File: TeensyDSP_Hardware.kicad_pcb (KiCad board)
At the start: 2 copper layers, 100 x 50 mm, 57 parts, among them J1 AudioJack2, J2 AudioJack2, J3 Conn_01x04_Pin, SW2 SW_DPDT_x2, SW3 SW_SPDT, U1 TL071, U2 LTC1044, U3 TL071, U4 TL071, U5 TL071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

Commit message: final commit before change to single ended
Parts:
- removed C10, C11, C12, C13, C14, C7, C8, C9: C, Capacitor_THT:C_Disc_D4.3mm_W1.9mm_P5.00mm
- removed J2: AudioJack2, Connector_Audio:Jack_3.5mm_Ledino_KB3SPRS_Horizontal
- removed R13, R14, R15, R16, R17, R18, R19: R, Resistor_THT:R_Axial_DIN0207_L6.3mm_D2.5mm_P7.62mm_Horizontal
- removed U4, U5: TL071, Package_DIP:DIP-8_W7.62mm
- removed UI_Switch_B1: SW_SPDT, Button_Switch_THT:SW_Slide-03_Wuerth-WS-SLTV_10x2.5x6.4_P2.54mm
- added R6: R, Resistor_THT:R_Axial_DIN0207_L6.3mm_D2.5mm_P7.62mm_Horizontal, F.Cu at (72.4, 101.5)
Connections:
- U6 pad 36: unconnected-(U6-14_A0_TX3_SPDIF_OUT-Pad36) -> /AD0
- U6 pad 37: unconnected-(U6-15_A1_RX3_SPDIF_IN-Pad37) -> /AD1
- U6 pad 42: unconnected-(U6-20_A6_TX5_LRCLK1-Pad42) -> /AD6
- U6 pad 43: unconnected-(U6-21_A7_RX5_BCLK1-Pad43) -> /AD7
- U6 pad 44: unconnected-(U6-22_A8_CTX1-Pad44) -> /AD8
- U6 pad 51: unconnected-(U6-3V3-Pad51) -> +3V3
- U6 pad 52: unconnected-(U6-GND-Pad52) -> GND

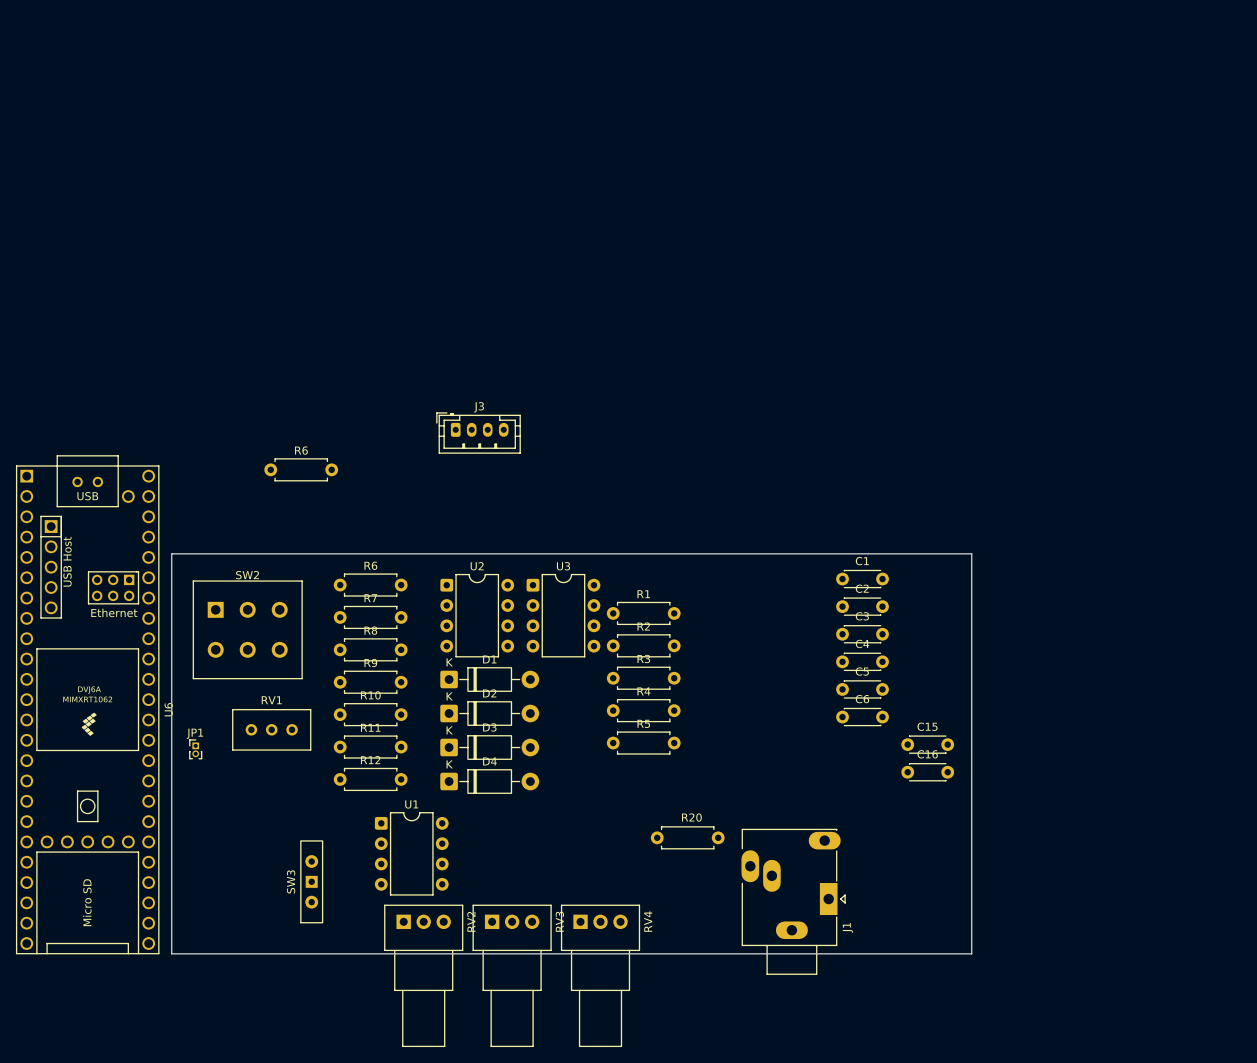
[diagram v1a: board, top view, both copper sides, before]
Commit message: First layout attempt - large footprint
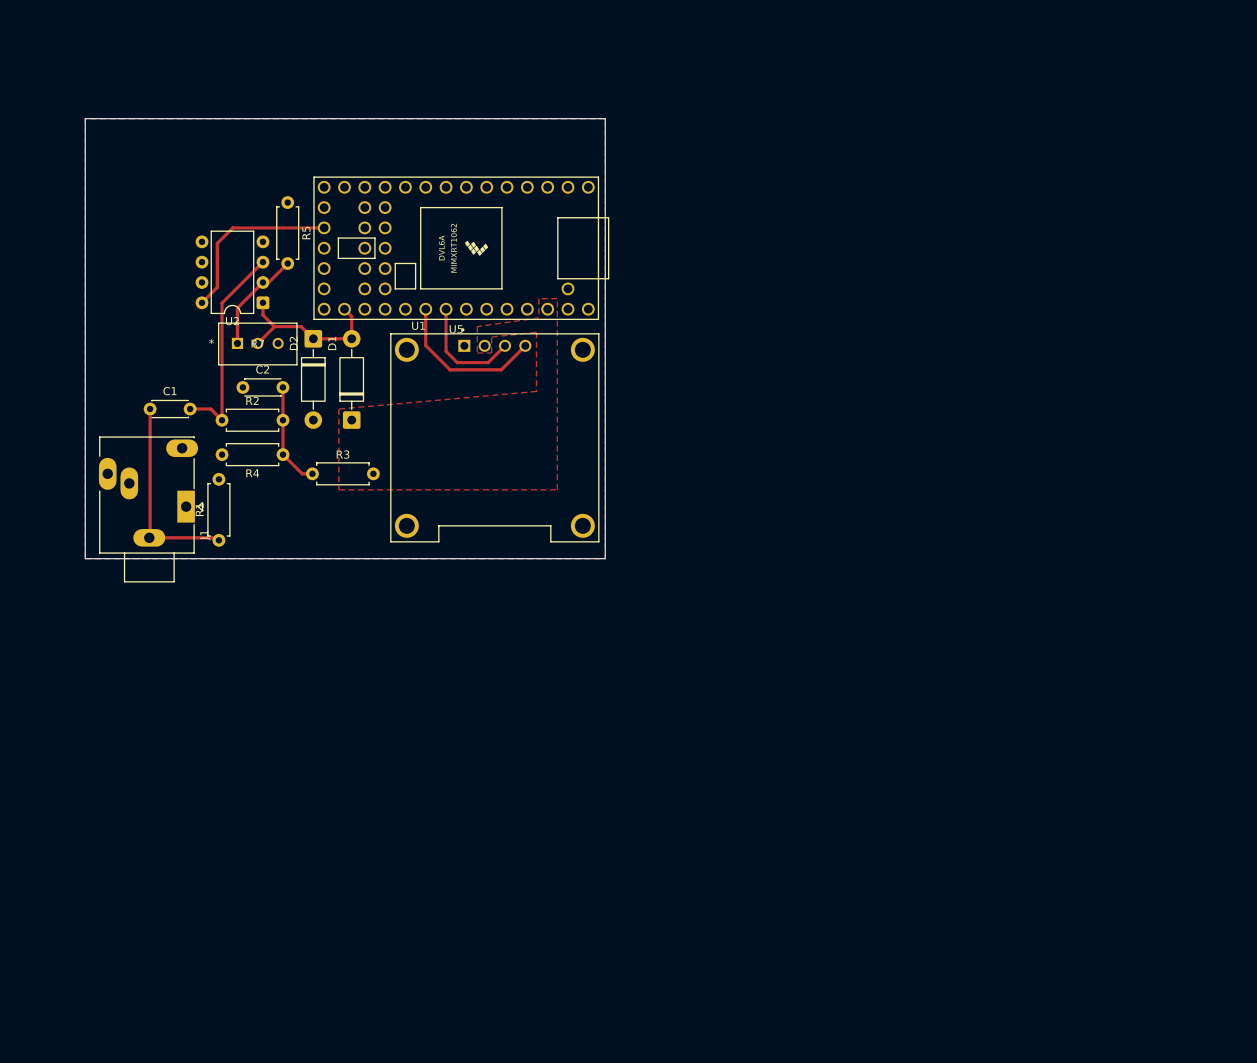
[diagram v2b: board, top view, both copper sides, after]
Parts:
- removed C15, C16, C3, C4, C5, C6: C, Capacitor_THT:C_Disc_D4.3mm_W1.9mm_P5.00mm
- removed D3, D4: 1N5817, Diode_THT:D_DO-41_SOD81_P10.16mm_Horizontal
- removed J3: Conn_01x04_Pin, Connector_JST:JST_PH_B4B-PH-K_1x04_P2.00mm_Vertical
- removed JP1: Jumper_2_Open, Connector_PinHeader_1.00mm:PinHeader_1x02_P1.00mm_Vertical
- removed R10, R11, R12, R20, R6 (x2), R8, R9: R, Resistor_THT:R_Axial_DIN0207_L6.3mm_D2.5mm_P7.62mm_Horizontal
- removed RV1: 500k, Potentiometer_THT:Potentiometer_Bourns_3296W_Vertical
- removed RV2, RV3, RV4: 500k, Potentiometer_THT:Potentiometer_Alps_RK09Y11_Single_Horizontal
- removed SW2: SW_DPDT_x2, Button_Switch_THT:SW_PUSH_E-Switch_FS5700DP_DPDT
- removed SW3: SW_SPDT, Button_Switch_THT:SW_Slide-03_Wuerth-WS-SLTV_10x2.5x6.4_P2.54mm
- removed U3: TL071, Package_DIP:DIP-8_W7.62mm
- removed U6: Teensy4.1, Teensy:Teensy41
- added U5: Teensy4.0, Teensy:Teensy40, F.Cu at (95.6, 73.8)
- C1, C2: value C -> 10u
- R1, R2: value R -> 47k
- R3: value R -> 10k
- R4: value R -> 2.2k
- R5: value R -> 1k
- R7: value R -> PV36W502C01B00; footprint Resistor_THT:R_Axial_DIN0207_L6.3mm_D2.5mm_P7.62mm_Horizontal -> MyComponents:POT_PV36W_BRN
- U1: value TL071 -> DM-OLED096-636; footprint Package_DIP:DIP-8_W7.62mm -> MyComponents:LED_SCREEN096
- U2: value LTC1044 -> TL072
- moved J1 94.1 mm to (61.8, 106.1)
- moved C1 89.1 mm to (57.3, 93.9)
- moved C2 79.8 mm to (68.9, 91.2)
- moved R5 78.9 mm to (74.5, 68.1), turned to -90 degrees
- moved R2 56.4 mm to (66.3, 95.3)
- moved R4 52.2 mm to (73.9, 99.6), turned to 180 degrees
- moved U1 50.2 mm to (100.4, 97.5)
- moved R1 50.1 mm to (65.9, 110.3), turned to 90 degrees
- moved D2 49.8 mm to (77.7, 85.1), turned to -90 degrees
- moved R3 45.5 mm to (77.6, 102.0)
- moved U2 42.1 mm to (71.4, 80.6), turned to 180 degrees
- moved R7 36.6 mm to (68.2, 85.7)
- moved D1 34.6 mm to (82.5, 95.3), turned to 90 degrees
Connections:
- C1 pad 1: /FX_In -> Net-(C1-Pad1)
- C1 pad 2: Net-(C1-Pad2) -> Net-(U2A-+)
- C2 pad 1: Net-(U1--) -> GND
- C2 pad 2: /IN_BUFFERED -> Net-(C2-Pad2)
- D1 pad 2: /AD0 -> /A0
- D2 pad 1: /AD0 -> /A0
- J1 pad S: /Input_Jack -> Net-(C1-Pad1)
- R1 pad 1: /FX_In -> Net-(C1-Pad1)
- R2 pad 1: Net-(C1-Pad2) -> Net-(U2A-+)
- R2 pad 2: Net-(JP1-A) -> Net-(C2-Pad2)
- R3 pad 1: Net-(C1-Pad2) -> Net-(C2-Pad2)
- R3 pad 2: Net-(U1-+) -> +3V3
- R4 pad 1: Net-(U1--) -> Net-(C2-Pad2)
- R4 pad 2: /IN_BUFFERED -> GND
- R5 pad 1: Net-(C3-Pad1) -> GND
- R5 pad 2: Net-(R5-Pad2) -> Net-(U2A--)
- R7 pad 1: GND -> Net-(U2A--)
- R7 pad 2: Net-(JP1-A) -> /A0
- U1 pad 1: unconnected-(U1-NULL-Pad1) -> GND
- U1 pad 2: Net-(U1--) -> +3V3
- U1 pad 3: Net-(U1-+) -> /SCL
- U1 pad 4: -5V -> /SDA
- U2 pad 1: +5V -> /A0
- U2 pad 2: Net-(U2-CAP+) -> Net-(U2A--)
- U2 pad 3: GND -> Net-(U2A-+)
- U2 pad 4: Net-(U2-CAP-) -> GND
- U2 pad 5: -5V -> unconnected-(U2B-+-Pad5)
- U2 pad 8: +5V -> +3V3
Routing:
- net Net-(U2A-+): track 0.00 -> 26.4 mm
- net Net-(C1-Pad1): track 0.00 -> 25.0 mm
- net +3V3: track 0.00 -> 22.4 mm
- net /A0: track 0.00 -> 20.9 mm
- net /SDA: track 0.00 -> 19.5 mm
- net /SCL: track 0.00 -> 14.1 mm
- net Net-(C2-Pad2): track 0.00 -> 13.1 mm
- net Net-(U2A--): track 0.00 -> 13.0 mm
- added copper zone on F.Cu, net +3V3
- added copper zone on B.Cu, net GND
- added copper zone on F.Cu, net GND
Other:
- board size 100 x 50 mm -> 65 x 55 mm

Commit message: move toward guitar tuner
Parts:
- added J2: Conn_01x02_Socket, Connector_JST:JST_EH_B2B-EH-A_1x02_P2.50mm_Vertical, B.Cu at (127.5, 75.8)
- added REF**: MountingHole_2.2mm_M2_DIN965_Pad, MountingHole:MountingHole_2.2mm_M2_DIN965_Pad, F.Cu at (187.5, 53.5)
- U5: moved to B.Cu
- moved R1 131.9 mm to (188.6, 61.8), turned to 180 degrees
- moved J1 129.0 mm to (184.2, 65.5), turned to 180 degrees
- moved C1 117.7 mm to (173.8, 77.0), turned to 90 degrees
- moved R2 110.2 mm to (173.5, 69.6), turned to 90 degrees
- moved R4 105.7 mm to (170.1, 55.8)
- moved C2 102.3 mm to (163.8, 52.8)
- moved R3 102.0 mm to (170.1, 59.0), turned to 180 degrees
- moved R5 96.4 mm to (170.8, 73.0), turned to 180 degrees
- moved U2 91.6 mm to (162.4, 69.6), turned to 90 degrees
- moved R7 85.1 mm to (152.8, 75.8), turned to 180 degrees
- moved D2 82.8 mm to (159.0, 69.3), turned to 90 degrees
- moved D1 81.7 mm to (155.8, 59.2), turned to -90 degrees
- moved U1 45.7 mm to (131.7, 64.1)
- moved U5 42.1 mm to (136.6, 64.0), turned to 0 degrees
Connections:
- U5 pad 33: unconnected-(U5-VIN-Pad33) -> Net-(J2-Pin_1)
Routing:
- net Net-(U2A-+): track 26.4 -> 9.77 mm
- net Net-(J2-Pin_1): track 0.00 -> 9.17 mm
- net /SCL: track 14.1 -> 21.3 mm
- net /A0: track 20.9 -> 17.2 mm
- net Net-(U2A--): track 13.0 -> 15.6 mm
- net Net-(C1-Pad1): track 25.0 -> 26.8 mm
- net /SDA: track 19.5 -> 21.3 mm
- net Net-(C2-Pad2): track 13.1 -> 11.5 mm
- net +3V3: track 22.4 -> 21.4 mm
- net GND: vias 0 -> 41
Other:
- board size 65 x 55 mm -> 71.5 x 27.5 mm

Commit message: Ordered Guitar Tuner
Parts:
- added J3: ChargerBoard, Connector_PinHeader_2.54mm:PinHeader_1x02_P2.54mm_Vertical, F.Cu at (127.5, 75.8)
- added J4: BatteryConnector, Connector_PinHeader_2.54mm:PinHeader_1x02_P2.54mm_Vertical, F.Cu at (176.0, 48.8)
- added R6: 10k, Resistor_SMD:R_0603_1608Metric, B.Cu at (151.4, 54.2)
- added REF**: MountingHole_2.2mm_M2_DIN965_Pad, MountingHole:MountingHole_2.2mm_M2_DIN965_Pad, F.Cu at (187.5, 77.0)
- added REF**: MountingHole_2.2mm_M2_DIN965_Pad, MountingHole:MountingHole_2.2mm_M2_DIN965_Pad, F.Cu at (120.5, 49.0)
- added SW1: SW_Push, Button_Switch_SMD:SW_SPST_B3U-3000P, B.Cu at (154.0, 48.2)
- J1: value AudioJack2 -> SJ1-3525N; footprint Connector_Audio:Jack_3.5mm_Ledino_KB3SPRS_Horizontal -> MyComponents:CUI_SJ1-3525N
- J2: footprint Connector_JST:JST_EH_B2B-EH-A_1x02_P2.50mm_Vertical -> Connector_JST:JST_PH_B2B-PH-K_1x02_P2.00mm_Vertical
- moved J2 59.0 mm to (180.7, 50.2)
- moved R1 4.75 mm to (188.6, 57.0)
- moved REF** 4.50 mm to (187.5, 49.0)
- moved J1 2.39 mm to (186.5, 64.8), turned to 90 degrees
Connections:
- J2 pad 1: Net-(J2-Pin_1) -> +BATT
- U5 pad 13: unconnected-(U5-11_MOSI_CTX1-Pad13) -> Net-(U5-11_MOSI_CTX1)
- U5 pad 33: Net-(J2-Pin_1) -> Net-(J3-Pin_1)
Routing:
- net +3V3: track 21.4 -> 32.4 mm
- net Net-(J3-Pin_1): track 0.00 -> 9.17 mm
- net Net-(J2-Pin_1): track 9.17 -> 0.00 mm
- net Net-(U5-11_MOSI_CTX1): track 0.00 -> 8.87 mm
- net Net-(C1-Pad1): track 26.8 -> 27.3 mm
- net GND: vias 41 -> 42
- added copper zone on In1.Cu, net GND
- added copper zone on In2.Cu, net GND
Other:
- board size 71.5 x 27.5 mm -> 72 x 33 mm
- copper layers 2 -> 4
- board text added: "10k"
- board text added: "10u"
- board text added: "1k"
- board text added: "2.2k"
- board text added: "47k"
- board text added: "BATT"
- board text added: "GuitarChoonah!"
